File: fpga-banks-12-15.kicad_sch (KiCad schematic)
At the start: 3 parts, among them U3002 XC7K160T-FFG676

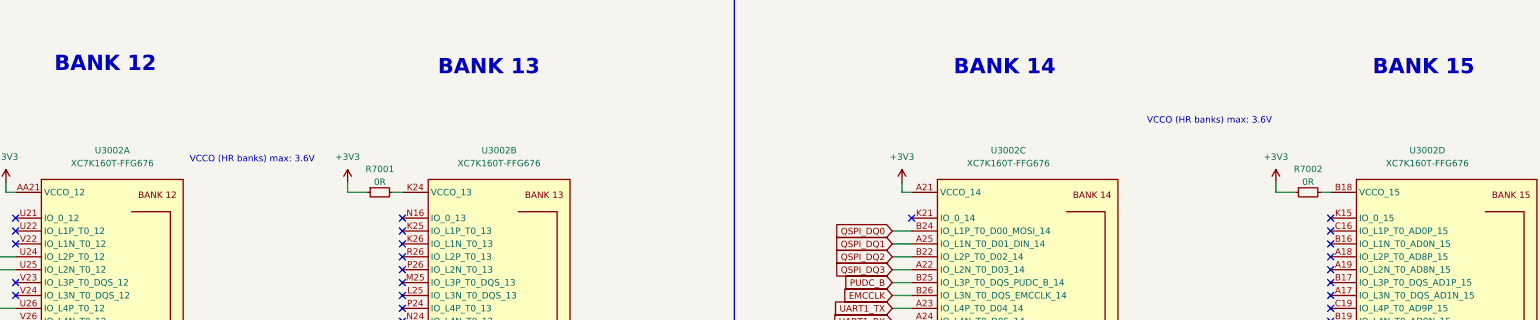
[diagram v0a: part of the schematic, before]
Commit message: Re-annotate schematic
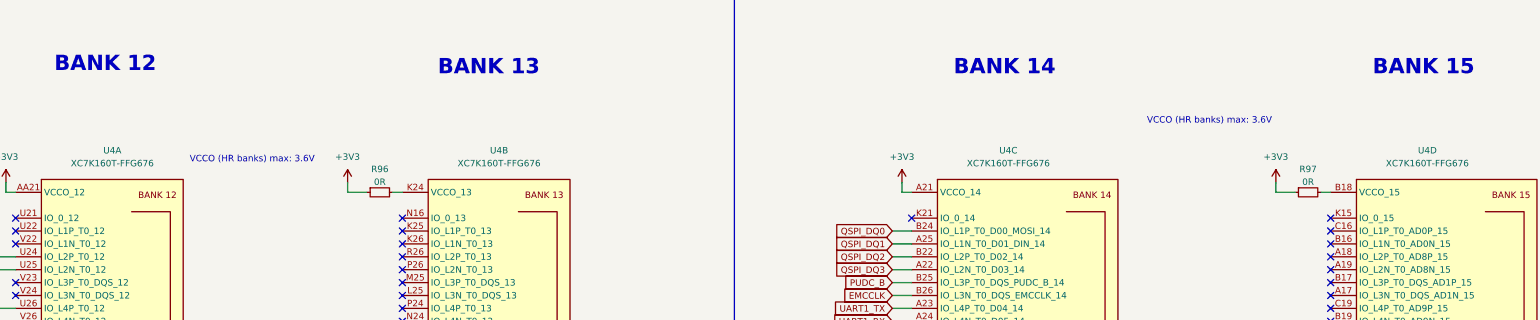
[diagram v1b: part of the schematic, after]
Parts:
- renumbered R7001 to R96, R7002 to R97, U3002 to U4
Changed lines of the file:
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@@
   (symbol (lib_id "sodimm-ddr5-tester:XC7K160T-FFG676") (at 68.58 86.995 0) (unit 1)
     (in_bom yes) (on_board yes) (fields_autoplaced)
-    (property "Reference" "U3002" (id 0) (at 87.63 78.74 0))
+    (property "Reference" "U4" (id 0) (at 87.63 78.74 0))
     (property "Value" "XC7K160T-FFG676" (id 1) (at 87.63 81.28 0)
       (effects (font (size 1.27 1.27) (thickness 0.15)))
@@
   (symbol (lib_id "sodimm-ddr5-tester:XC7K160T-FFG676") (at 144.78 86.995 0) (unit 2)
     (in_bom yes) (on_board yes) (fields_autoplaced)
-    (property "Reference" "U3002" (id 0) (at 163.83 78.74 0))
+    (property "Reference" "U4" (id 0) (at 163.83 78.74 0))
     (property "Value" "XC7K160T-FFG676" (id 1) (at 163.83 81.28 0)
       (effects (font (size 1.27 1.27) (thickness 0.15)))
@@
   (symbol (lib_id "antmicroResistors0402:R_0R_0402") (at 320.675 86.995 0) (unit 1)
     (in_bom yes) (on_board yes) (fields_autoplaced)
-    (property "Reference" "R7002" (id 0) (at 323.215 82.421 0)
+    (property "Reference" "R97" (id 0) (at 323.215 82.421 0)
       (effects (font (size 1.27 1.27) (thickness 0.15)))
     )
@@
   (symbol (lib_id "sodimm-ddr5-tester:XC7K160T-FFG676") (at 327.66 86.995 0) (unit 4)
     (in_bom yes) (on_board yes) (fields_autoplaced)
-    (property "Reference" "U3002" (id 0) (at 346.71 78.74 0))
+    (property "Reference" "U4" (id 0) (at 346.71 78.74 0))
     (property "Value" "XC7K160T-FFG676" (id 1) (at 346.71 81.28 0)
       (effects (font (size 1.27 1.27) (thickness 0.15)))
@@
   (symbol (lib_id "sodimm-ddr5-tester:+3V3") (at 66.675 85.09 0) (unit 1)
     (in_bom yes) (on_board yes) (fields_autoplaced)
-    (property "Reference" "#PWR0164" (id 0) (at 66.675 88.9 0)
+    (property "Reference" "#PWR0235" (id 0) (at 66.675 88.9 0)
       (effects (font (size 1.27 1.27)) hide)
     )
@@
   (symbol (lib_id "sodimm-ddr5-tester:+3V3") (at 243.205 85.09 0) (unit 1)
     (in_bom yes) (on_board yes) (fields_autoplaced)
-    (property "Reference" "#PWR0163" (id 0) (at 243.205 88.9 0)
+    (property "Reference" "#PWR0237" (id 0) (at 243.205 88.9 0)
       (effects (font (size 1.27 1.27)) hide)
     )
@@
   (symbol (lib_id "antmicroResistors0402:R_0R_0402") (at 137.795 86.995 0) (unit 1)
     (in_bom yes) (on_board yes) (fields_autoplaced)
-    (property "Reference" "R7001" (id 0) (at 140.335 82.421 0)
+    (property "Reference" "R96" (id 0) (at 140.335 82.421 0)
       (effects (font (size 1.27 1.27) (thickness 0.15)))
     )
@@
   (symbol (lib_id "sodimm-ddr5-tester:+3V3") (at 133.985 85.09 0) (unit 1)
     (in_bom yes) (on_board yes) (fields_autoplaced)
-    (property "Reference" "#PWR0290" (id 0) (at 133.985 88.9 0)
+    (property "Reference" "#PWR0236" (id 0) (at 133.985 88.9 0)
       (effects (font (size 1.27 1.27)) hide)
     )
@@
   (symbol (lib_id "sodimm-ddr5-tester:+3V3") (at 316.865 85.09 0) (unit 1)
     (in_bom yes) (on_board yes) (fields_autoplaced)
-    (property "Reference" "#PWR0289" (id 0) (at 316.865 88.9 0)
+    (property "Reference" "#PWR0238" (id 0) (at 316.865 88.9 0)
       (effects (font (size 1.27 1.27)) hide)
     )
@@
   (symbol (lib_id "sodimm-ddr5-tester:XC7K160T-FFG676") (at 245.11 86.995 0) (unit 3)
     (in_bom yes) (on_board yes) (fields_autoplaced)
-    (property "Reference" "U3002" (id 0) (at 264.16 78.74 0))
+    (property "Reference" "U4" (id 0) (at 264.16 78.74 0))
     (property "Value" "XC7K160T-FFG676" (id 1) (at 264.16 81.28 0)
       (effects (font (size 1.27 1.27) (thickness 0.15)))

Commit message: Add local libraries
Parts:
- R96, R97: footprint antmicro-footprints:R_0402_1005Metric_EIA -> sodimm-ddr5-tester-footprints:R_0402_1005Metric_EIA; symbol antmicroResistors0402:R_0R_0402 -> sodimm-ddr5-tester:R_0R_0402

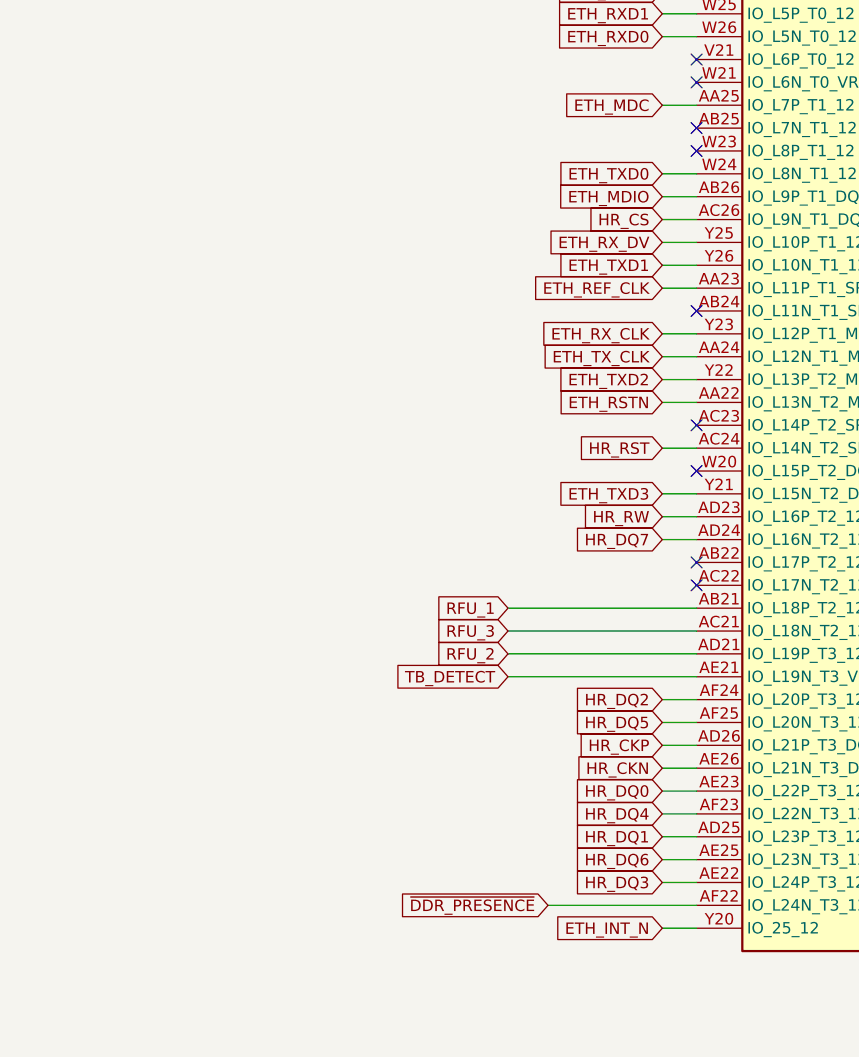
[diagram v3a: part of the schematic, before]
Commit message: Define DDR5, HyperBus and I2C buses. Connect HyperRAM with hierarchical bus
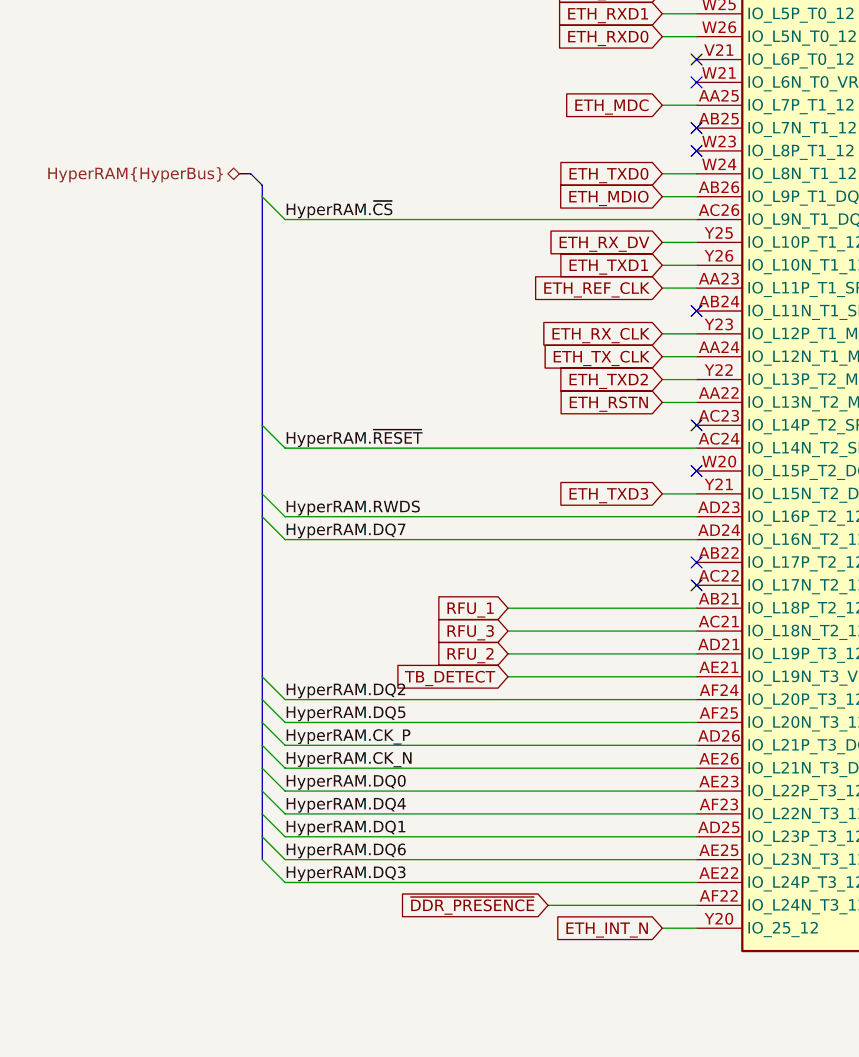
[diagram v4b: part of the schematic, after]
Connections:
- net HR_CKN renamed HyperRAM.CK_N
- net HR_CKP renamed HyperRAM.CK_P
- net HR_CS renamed HyperRAM.~{CS}
- net HR_DQ0 renamed HyperRAM.DQ0
- net HR_DQ1 renamed HyperRAM.DQ1
- net HR_DQ2 renamed HyperRAM.DQ2
- net HR_DQ3 renamed HyperRAM.DQ3
- net HR_DQ4 renamed HyperRAM.DQ4
- net HR_DQ5 renamed HyperRAM.DQ5
- net HR_DQ6 renamed HyperRAM.DQ6
- net HR_DQ7 renamed HyperRAM.DQ7
- net HR_RST renamed HyperRAM.~{RESET}
- net HR_RW renamed HyperRAM.RWDS

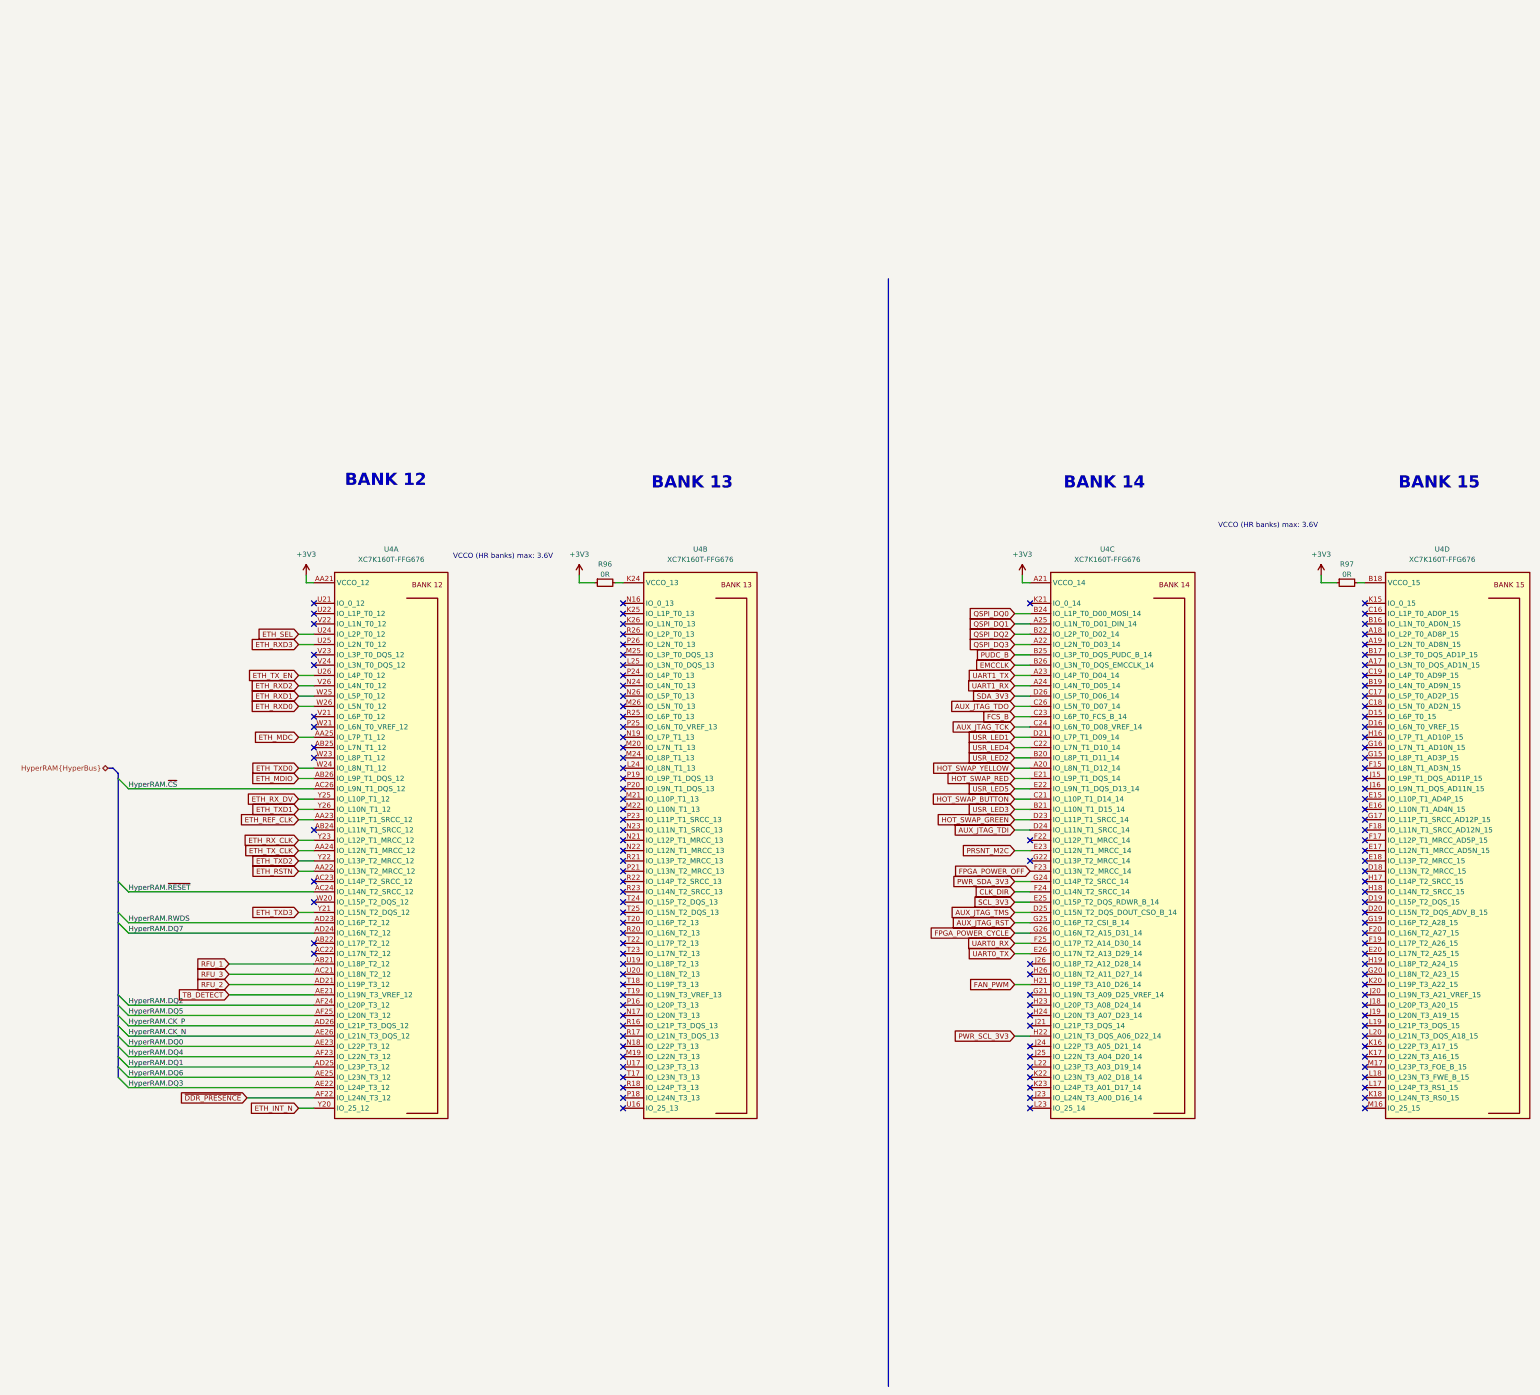
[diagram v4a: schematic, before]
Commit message: Connect DDR hierarchical labels. Define and connect JTAG, RGMII, TDMS, UART, and SDIO buses. Reorganize schematic blocks between sheets
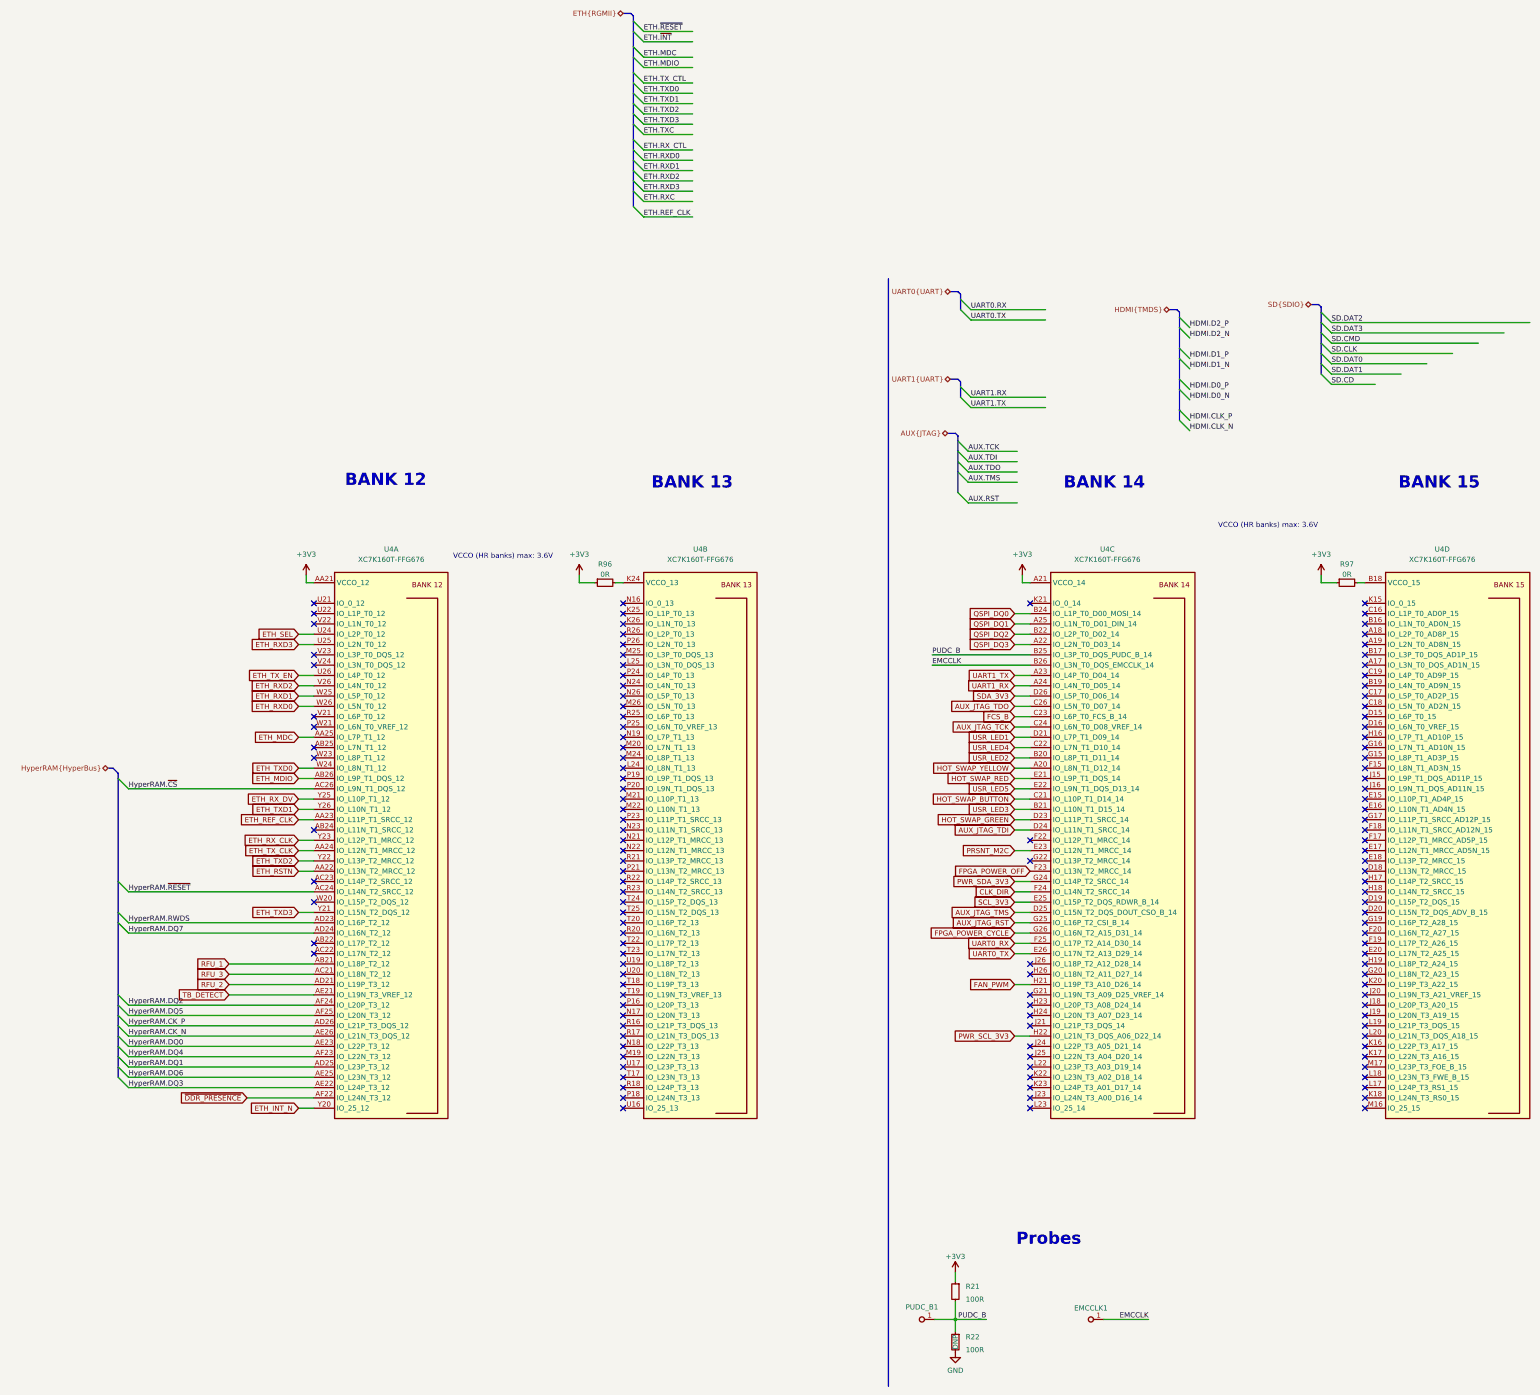
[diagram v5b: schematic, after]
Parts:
- added EMCCLK1, PUDC_B1: TP_1mm_SMD, sodimm-ddr5-tester-footprints:TP_SMD_1mm, symbol sodimm-ddr5-tester:TP_1mm_SMD
- added R21, R22: R_100R_0402, sodimm-ddr5-tester-footprints:R_0402_1005Metric, symbol sodimm-ddr5-tester:R_100R_0402
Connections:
- net +3V3: now also R21.1
- net EMCCLK: now also EMCCLK1.1
- net PUDC_B: now also PUDC_B1.1, R21.2, R22.1
- new net GND: R22.2
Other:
- note added: "Probes"
